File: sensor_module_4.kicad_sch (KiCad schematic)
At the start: 55 parts, among them J1 Conn_Coaxial, J15 SLOT 1, J3 Conn_Coaxial, J4 Conn_01x03_Socket, J5 Conn_01x02_Pin, U12 REF3025, U13 MCP3204, U16 74LVC1G3157, U30 TLV2387DR, U4 OPA2397DGKR, U5 OPA2397DGKR, U6 M24C02-WMN, U7 TPS22929D, U8 REF3040

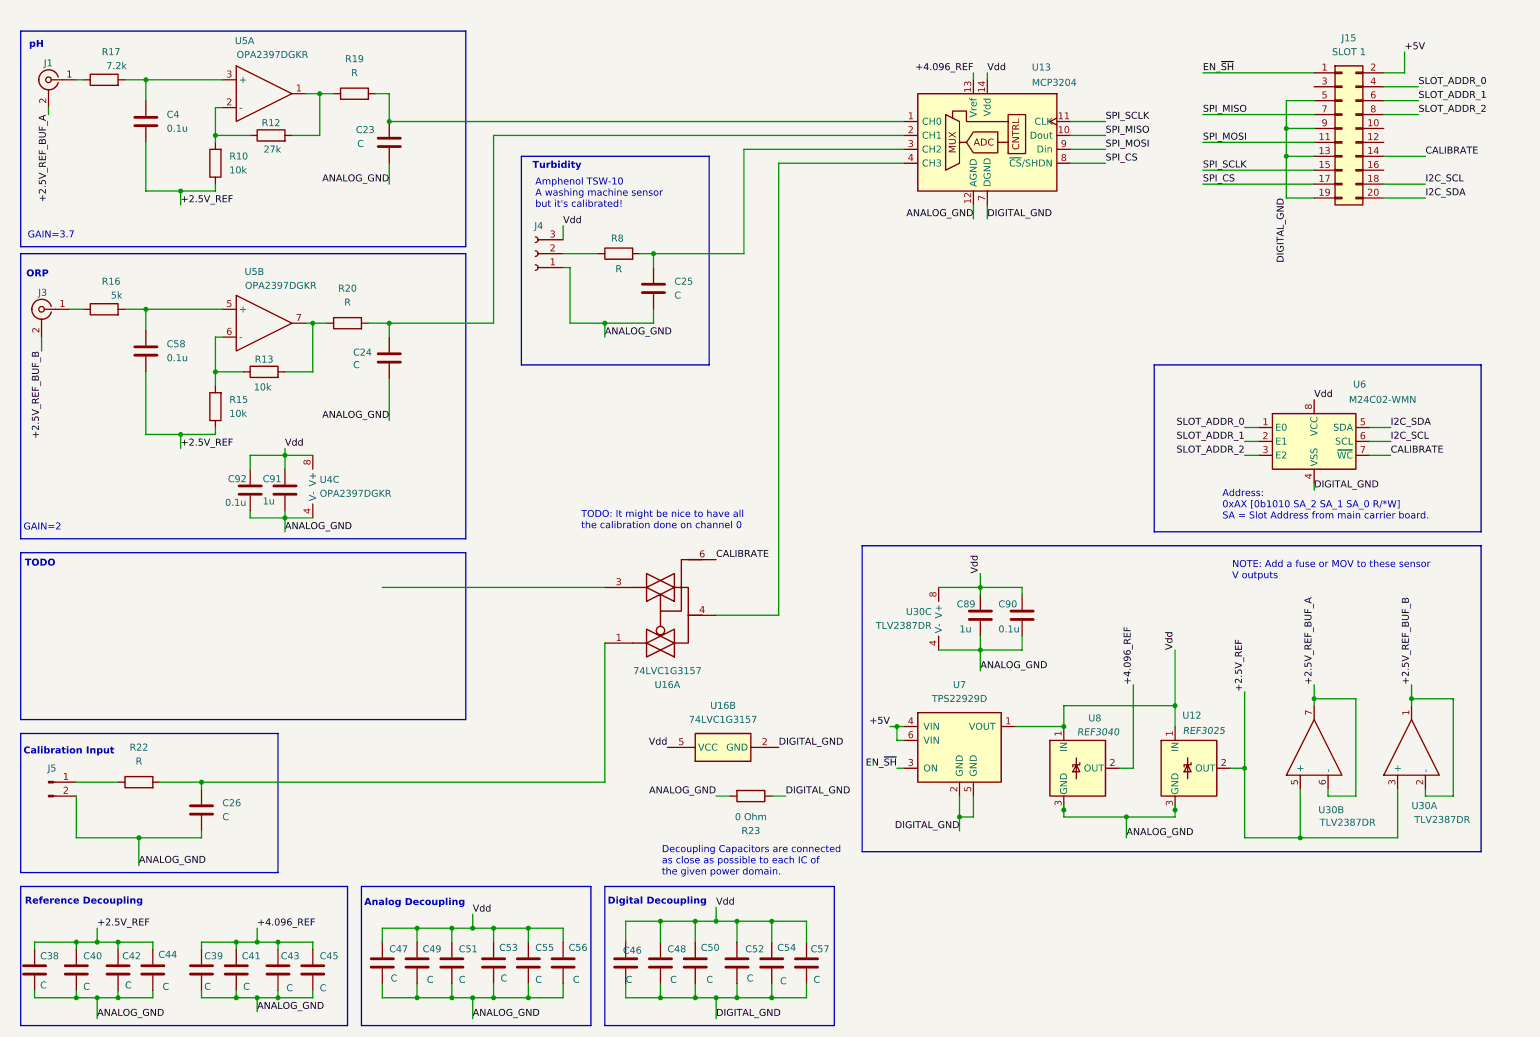
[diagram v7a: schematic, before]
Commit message: Began assigning footprints Cleaned up some of the signalling and added the full prototype sensor suite Added a header for the Atlas Scientific carrier board Added some test points and jumpers Cleaned up the power section Started work on the CPU signal assignment and header sockets
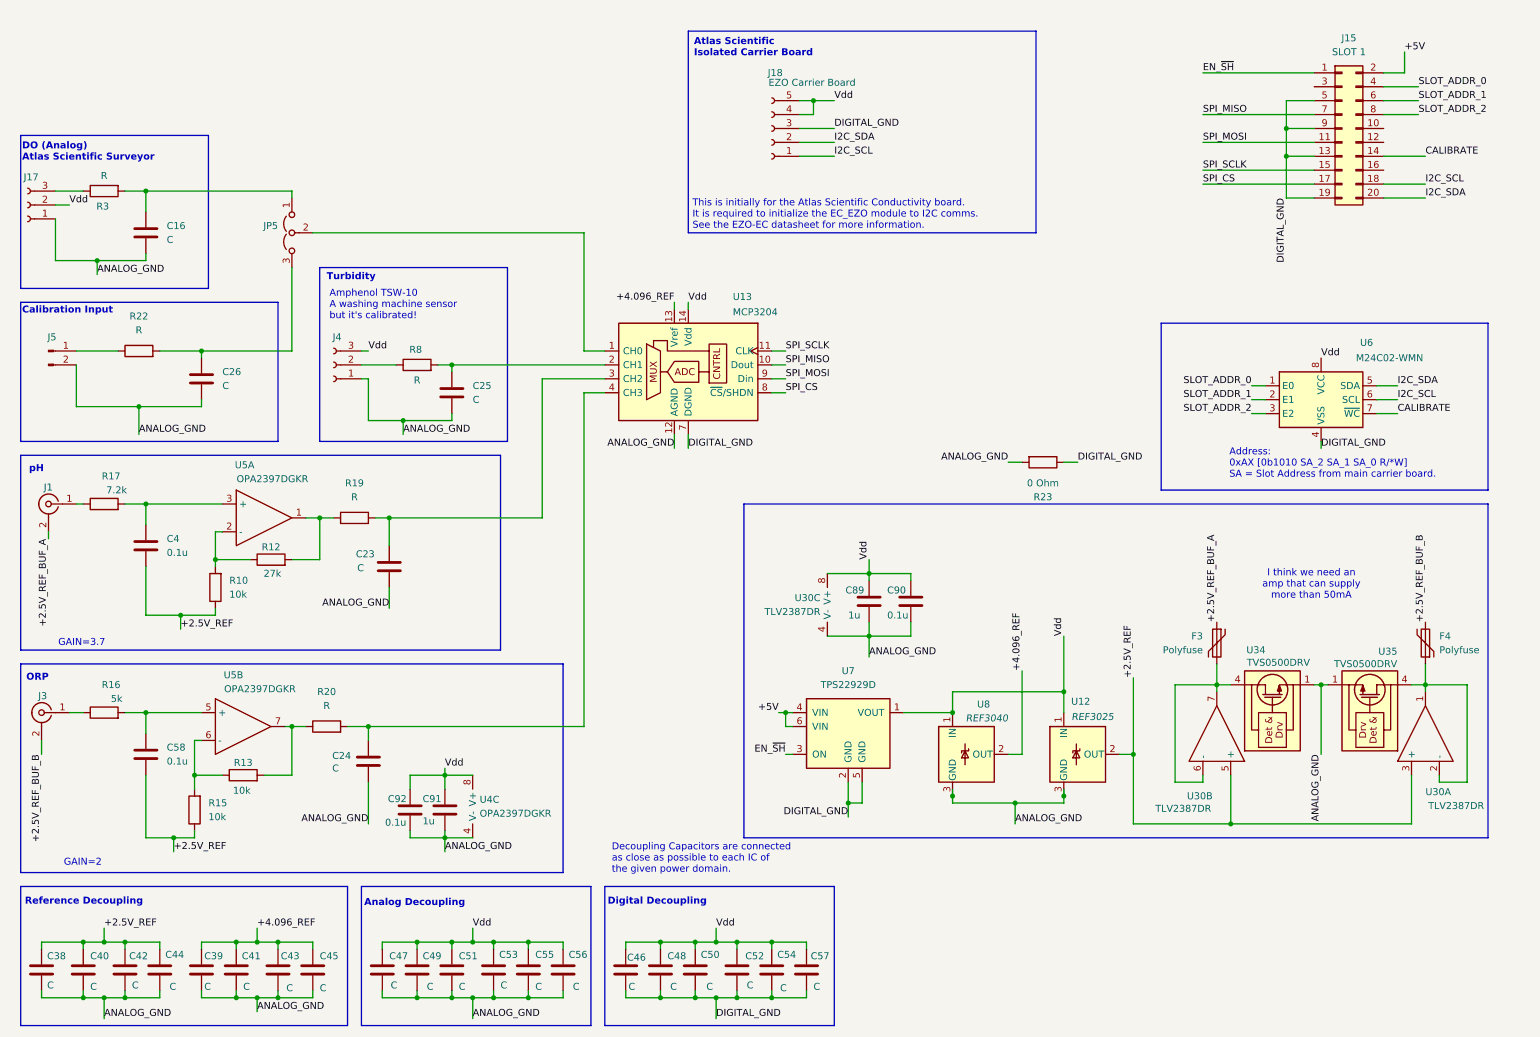
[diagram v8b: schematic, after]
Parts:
- removed U16: 74LVC1G3157, symbol 74xGxx:74LVC1G3157
- added C16: C, symbol Device:C
- added F3, F4: Polyfuse, symbol Device:Polyfuse
- added J17: Conn_01x03_Socket, symbol Connector:Conn_01x03_Socket
- added J18: EZO Carrier Board, Connector_PinHeader_1.27mm:PinHeader_1x05_P1.27mm_Horizontal, symbol Connector:Conn_01x05_Socket
- added JP5: Jumper_3_Open, symbol Jumper:Jumper_3_Open
- added R3: R, symbol Device:R
- added U34, U35: TVS0500DRV, Package_SON:WSON-6-1EP_2x2mm_P0.65mm_EP1x1.6mm, symbol Power_Protection:TVS0500DRV
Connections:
- net +2.5V_REF_BUF_A: now also F3.1; no longer U30.6 (-), U30.7
- net +2.5V_REF_BUF_B: now also F4.2; no longer U30.1, U30.2 (-)
- net ANALOG_GND: now also C16.2, J17.1 (Pin_1), U34.1 (GND), U34.2 (GND), U34.3 (GND), U34.7 (GND), U35.1 (GND), U35.2 (GND), U35.3 (GND), U35.7 (GND)
- net DIGITAL_GND: now also J18.3 (Pin_3)
- net I2C_SCL: now also J18.1 (Pin_1)
- net I2C_SDA: now also J18.2 (Pin_2)
- net Vdd: now also J17.2 (Pin_2), J18.4 (Pin_4), J18.5 (Pin_5)
- net at C26.1, R22.2: now also JP5.3 (B)
- net at C23.1, R19.2: now also U13.3 (CH2); no longer U13.1 (CH0)
- net at C25.1, R8.2: now also U13.2 (CH1); no longer U13.3 (CH2)
- net at U13.4 (CH3): now also C24.1, R20.2
- new net: F3.2, U30.6 (-), U30.7, U34.4 (IN), U34.5 (IN), U34.6 (IN)
- new net: F4.1, U30.1, U30.2 (-), U35.4 (IN), U35.5 (IN), U35.6 (IN)
- new net: J17.3 (Pin_3), R3.1
- new net: C16.1, JP5.1 (A), R3.2
- new net: JP5.2 (C), U13.1 (CH0)
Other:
- note added: "DO (Analog) Atlas Scientific Surveyor"
- note added: "I think we need an amp that can supply more than 50mA"
- note added: "This is initially for the Atlas Scientific Conductivity board. It is required to initialize the EC_EZO module to I2C comms. See the EZO-EC datasheet for more information."
- note removed: "NOTE: Add a fuse or MOV to these sensor V outputs"
- note removed: "TODO"
- note removed: "TODO: It might be nice to have all the calibration done on channel 0"
- moved on the sheet: C23, C24, C25, C26, C38, C4, C40, C42, C44, C46, C47, C48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
